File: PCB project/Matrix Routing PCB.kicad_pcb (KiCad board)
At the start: 4 copper layers, 87 x 35 mm, 14 parts, among them J1 Connector 1x6, J2 JST_PH_S4B-PH-SM4-TB_1x04-1MP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, J3 ESQ-105-11-T-D, J4 TSM-102-01-L-DH-A, J5 USB-A-S-X-X-SM2-R, U1 FT232RL

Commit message: V1 prepare for generating the manufacturing files
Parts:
- C1, C3: value C -> 100nF
- C2: value C -> 10nF
- C4: value C -> 4.7uF
- J1: value Connector 1x6 -> 53261-0471
- J2: value JST_PH_S4B-PH-SM4-TB_1x04-1MP_P2.00mm_Horizontal -> JST_PH_S4B-PH-SM4-TB
- J3: value ESQ-105-11-T-D -> ESQ-105-12-T-D
- J5: value USB-A-S-X-X-SM2-R -> USB-A-S-F-B-SM2-R-TR
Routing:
- net /USB1_DP: track 58.2 -> 54.2 mm
- net /USB1_DN: track 57.3 -> 53.3 mm
- net /USB2_DN: track 34.2 -> 32.2 mm
- net /USB2_DP: track 32.9 -> 30.8 mm
- net GND: track 42.4 -> 44.1 mm
- net /TX_FTDI_RX_BOARD: track 48.9 -> 50.0 mm
- net +5V: track 13.3 -> 14.2 mm
- net VBUS: track 8.86 -> 9.63 mm
- net /RX_FTDI_TX_BOARD: track 56.9 -> 56.3 mm
- added copper zone on F.Cu, net GND
- added copper zone on In2.Cu, net GND

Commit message: Fix 3D conflicts
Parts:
- moved FID1 33.1 mm to (211.7, 76.6)
- moved FID2 10.5 mm to (189.2, 102.7)
- moved C3 6.10 mm to (238.1, 94.3)
- moved C4 6.10 mm to (239.6, 94.3)
- moved U1 6.10 mm to (231.8, 95.8)
- moved C1 6.10 mm to (238.1, 98.4)
- moved C2 6.10 mm to (225.6, 94.5)
- moved J2 2.31 mm to (179.9, 94.9)
- moved H1 0.75 mm to (203.2, 76.6)
- moved J5 0.75 mm to (191.7, 81.8)
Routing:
- net /USB2_DP: track 30.8 -> 36.9 mm
- net /USB2_DN: track 32.2 -> 38.3 mm
- net /USB1_DN: track 53.3 -> 58.7 mm
- net /USB1_DP: track 54.2 -> 59.5 mm
- net /RX_FTDI_TX_BOARD: track 56.3 -> 58.9 mm
- net /TX_FTDI_RX_BOARD: track 50.0 -> 52.3 mm
- net /USB_OTG_DP: track 82.5 -> 83.3 mm
- net /USB_OTG_DN: track 82.5 -> 83.3 mm

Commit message: Fix J5 potition
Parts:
- moved H1 0.79 mm to (202.4, 76.6)
- moved J5 0.79 mm to (190.9, 81.8)
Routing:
- net /USB_OTG_DP: track 83.3 -> 84.1 mm
- net /USB_OTG_DN: track 83.3 -> 84.1 mm

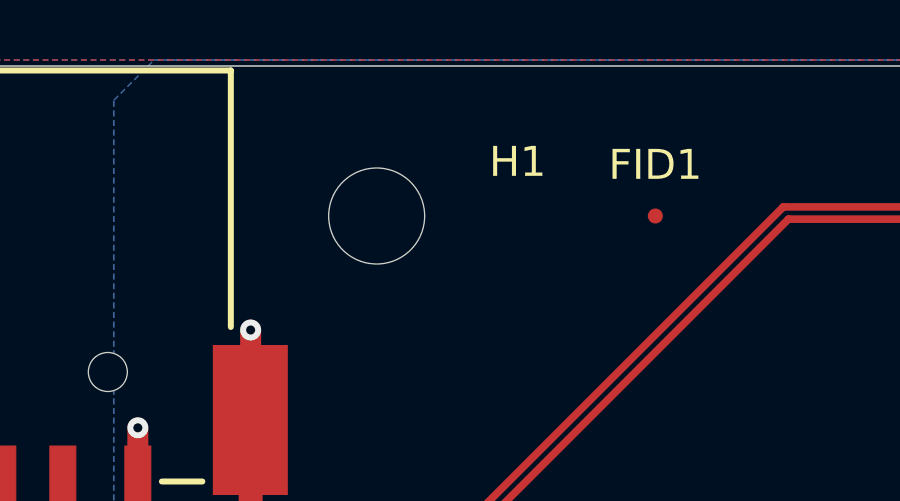
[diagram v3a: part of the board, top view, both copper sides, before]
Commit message: Version for Review, long connector is too short
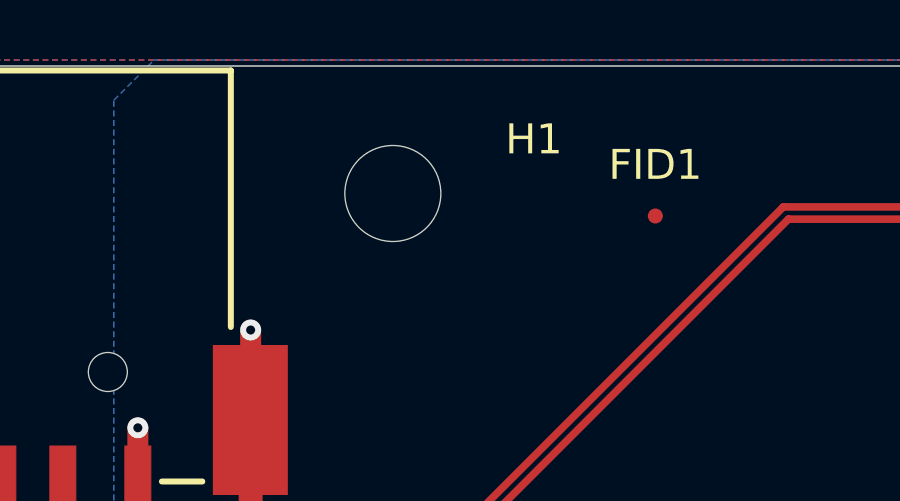
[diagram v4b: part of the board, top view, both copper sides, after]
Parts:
- moved H1 0.92 mm to (202.9, 75.8)
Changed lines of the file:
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@@
 	(footprint "MountingHole:MountingHole_3.2mm_M3"
 		(layer "F.Cu")
-		(at 202.360425 76.575)
+		(at 202.9 75.825)
 		(descr "Mounting Hole 3.2mm, M3, no annular, generated by kicad-footprint-generator mountinghole.py")
 		(tags "mountinghole M3")
